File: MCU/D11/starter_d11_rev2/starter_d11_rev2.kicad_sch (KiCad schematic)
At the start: 22 parts, among them J1 USB_A, J2 SWD-5, J3 Data, J4 out_5V0, J5 out_3V3, SW1 Reset, U1 ATSAMD11C14A-SS, U2 PRTR5V0, U3 TLV73333/SOT-23, X1 ECS-2520MV-xxx-xx

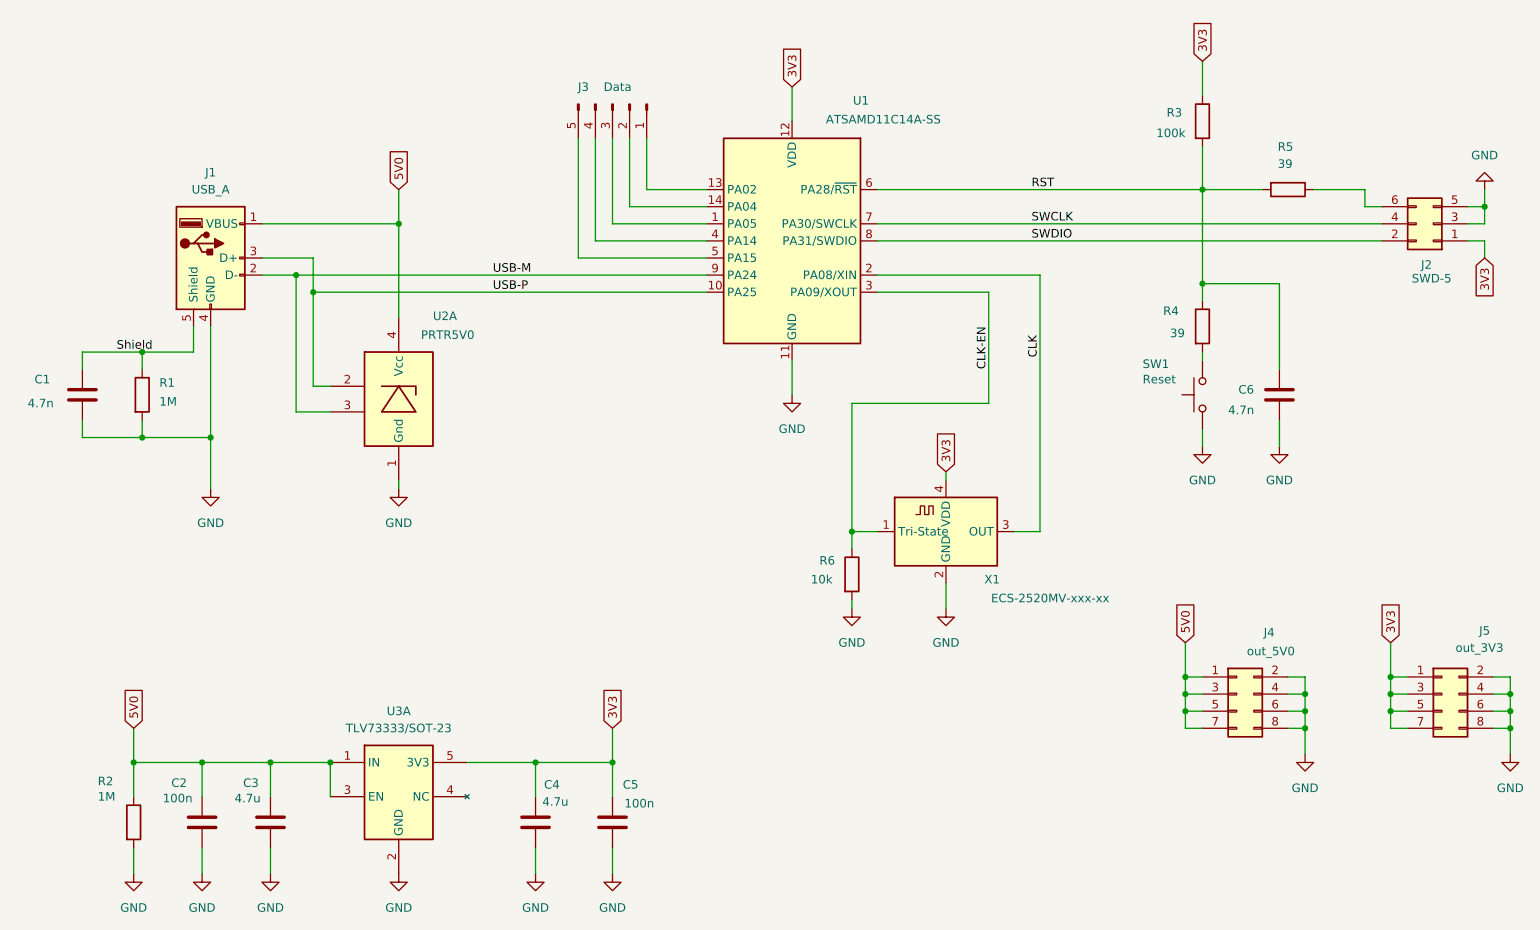
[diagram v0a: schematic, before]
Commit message: D11 project is split into pages Transistors updated in PWM and Thyristor
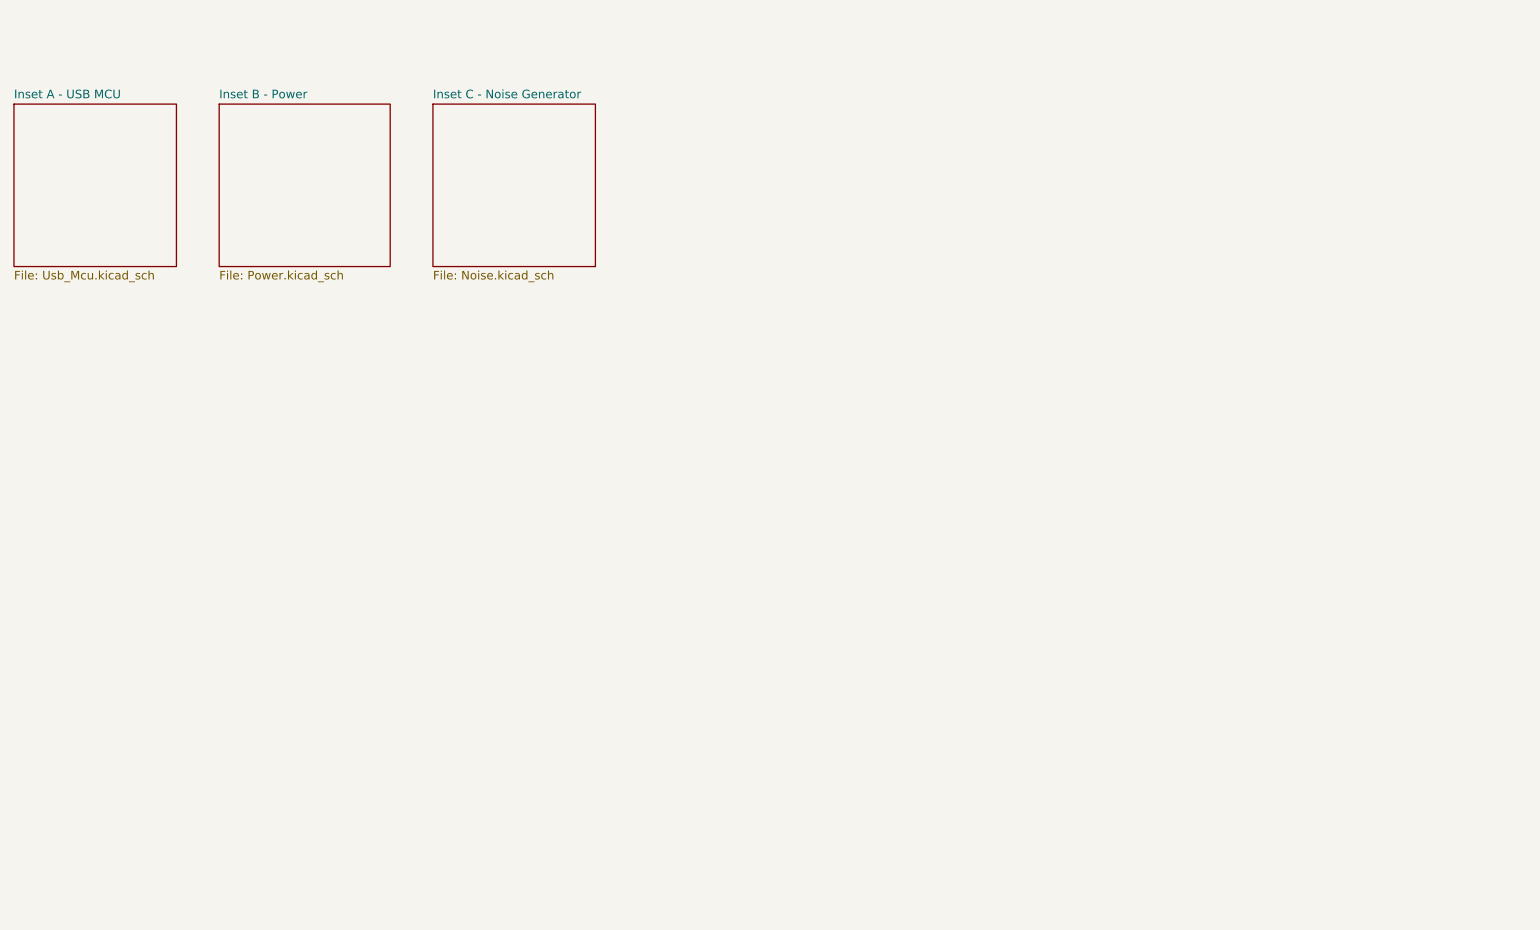
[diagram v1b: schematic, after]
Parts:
- removed C1, C6: 4.7n, Capacitor_SMD:C_0805_2012Metric_Pad1.18x1.45mm_HandSolder, symbol Device:C
- removed C2, C5: 100n, Capacitor_SMD:C_0805_2012Metric_Pad1.18x1.45mm_HandSolder, symbol Device:C
- removed C3, C4: 4.7u, Capacitor_SMD:C_0805_2012Metric_Pad1.18x1.45mm_HandSolder, symbol Device:C
- removed J1: USB_A, Connector_USB:USB_A_Molex_48037-2200_Horizontal, symbol Connector:USB_A
- removed J2: SWD-5, Connector_PinSocket_1.27mm:PinSocket_2x03_P1.27mm_Vertical, symbol Connector_Generic:Conn_02x03_Odd_Even
- removed J3: Data, Connector_PinHeader_2.54mm:PinHeader_1x05_P2.54mm_Vertical, symbol Connector:Conn_01x05_Pin
- removed J4: out_5V0, Connector_PinHeader_2.54mm:PinHeader_2x04_P2.54mm_Vertical, symbol Connector_Generic:Conn_02x04_Odd_Even
- removed J5: out_3V3, Connector_PinHeader_2.54mm:PinHeader_2x04_P2.54mm_Vertical, symbol Connector_Generic:Conn_02x04_Odd_Even
- removed R1, R2: 1M, Resistor_SMD:R_0805_2012Metric_Pad1.20x1.40mm_HandSolder, symbol Device:R
- removed R3: 100k, Resistor_SMD:R_0805_2012Metric_Pad1.20x1.40mm_HandSolder, symbol Device:R
- removed R4, R5: 39, Resistor_SMD:R_0805_2012Metric_Pad1.20x1.40mm_HandSolder, symbol Device:R
- removed R6: 10k, Resistor_SMD:R_0805_2012Metric_Pad1.20x1.40mm_HandSolder, symbol Device:R
- removed SW1: Reset, Button_Switch_SMD:SW_Tactile_SPST_NO_Straight_CK_PTS636Sx25SMTRLFS, symbol Switch:SW_Push
- removed U1: ATSAMD11C14A-SS, Package_SO:SOIC-14_3.9x8.7mm_P1.27mm, symbol MCU_Microchip_SAMD:ATSAMD11C14A-SS
- removed U2: PRTR5V0, Package_TO_SOT_SMD:SOT-143_Handsoldering, symbol Secoh:USB/PRTR5V0-SOT-143
- removed U3: TLV73333/SOT-23, Package_TO_SOT_SMD:SOT-23-5_HandSoldering, symbol Secoh:VRegs/TLV73333-SOT-23
- removed X1: ECS-2520MV-xxx-xx, Oscillator:Oscillator_SMD_ECS_2520MV-xxx-xx-4Pin_2.5x2.0mm, symbol Oscillator:ECS-2520MV-xxx-xx
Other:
- added sheet Inset A - USB MCU (Usb_Mcu.kicad_sch)
- added sheet Inset B - Power (Power.kicad_sch)
- added sheet Inset C - Noise Generator (Noise.kicad_sch)
